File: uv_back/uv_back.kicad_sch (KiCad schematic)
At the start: 1 part, among them U1 OPA1656ID

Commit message: roughed out the schematic
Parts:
- added C1, C2: 0.1uF, Resistor_SMD:R_0603_1608Metric, symbol Device:C
- added C3, C5: 10000pF, Capacitor_SMD:C_0603_1608Metric, symbol Device:C
- added C4: 1uF, Capacitor_SMD:C_0805_2012Metric, symbol Device:C
- added J1, J3, J7: B2B-PH-SM4-TB(LF)(SN), Connector_JST:JST_PH_B2B-PH-SM4-TB_1x02-1MP_P2.00mm_Vertical, symbol Connector_Generic:Conn_01x02
- added J2, J4, J5, J6, J8: B3B-PH-SM4-TB(LF)(SN), Connector_JST:JST_PH_B3B-PH-SM4-TB_1x03-1MP_P2.00mm_Vertical, symbol Connector_Generic:Conn_01x03
- added R1, R2: 10k, Resistor_SMD:R_0603_1608Metric, symbol Device:R_US
- added R10, R6, R8, R9: 2k, Resistor_SMD:R_0603_1608Metric, symbol Device:R_US
- added R11: 50, Resistor_SMD:R_0603_1608Metric, symbol Device:R_US
- added R3, R4: 0, Resistor_SMD:R_0603_1608Metric, symbol Device:R_US
- added R5, R7: 1k, Resistor_SMD:R_0603_1608Metric, symbol Device:R_US
- added U2: OPA1656ID, Package_SO:SOIC-8_3.9x4.9mm_P1.27mm, symbol eAudio_OpAmp:OPA1656ID
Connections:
- net at U1.1: now also C3.2, C4.1, R9.2
- net at U1.2 (-): now also C3.1, J5.2 (Pin_2), J6.2 (Pin_2), R9.1
- net VMID: now reaches U1.3 (+)
- net VMID: now also J2.3 (Pin_3), J4.3 (Pin_3), U2.1, U2.2 (-)
- net GND: now reaches U1.4 (V-)
- net GND: now also C1.1, C2.1, C5.1, J1.2 (Pin_2), J3.2 (Pin_2), J8.3 (Pin_3), R10.1, R2.1, U2.4 (V-)
- net +9V: now reaches U1.8 (V+)
- net +9V: now also C1.2, C2.2, J7.1 (Pin_1), R1.2, U2.8 (V+)
- net at U1.5 (+): now also J2.2 (Pin_2)
- net at U1.6 (-): now also U1.7, R3.1
- new net: C4.2, R10.2, R11.1
- new net: R3.2, R5.1, R6.1
- new net: J5.1 (Pin_1), R5.2
- new net: J1.1 (Pin_1), J2.1 (Pin_1)
- new net: R4.1, U2.6 (-), U2.7
- new net: R4.2, R7.1, R8.1
- new net: J3.1 (Pin_1), J4.1 (Pin_1)
- new net: J4.2 (Pin_2), U2.5 (+)
- new net: C5.2, R1.1, R2.2, U2.3 (+)
- new net: J6.1 (Pin_1), R7.2
- new net: J6.3 (Pin_3), R8.2
- new net: J5.3 (Pin_3), R6.2
- new net BATT-: J7.2 (Pin_2), J8.2 (Pin_2)
- new net SIG_OUT: J8.1 (Pin_1), R11.2
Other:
- note added: "MixMonkey"
- note added: "Ring"
- note added: "Sleeve"
- note added: "Tip"
- company: (none) -> Wavenumber LLC
- title: (none) -> MixMonkey
- moved on the sheet: U1A, U1B, U1C

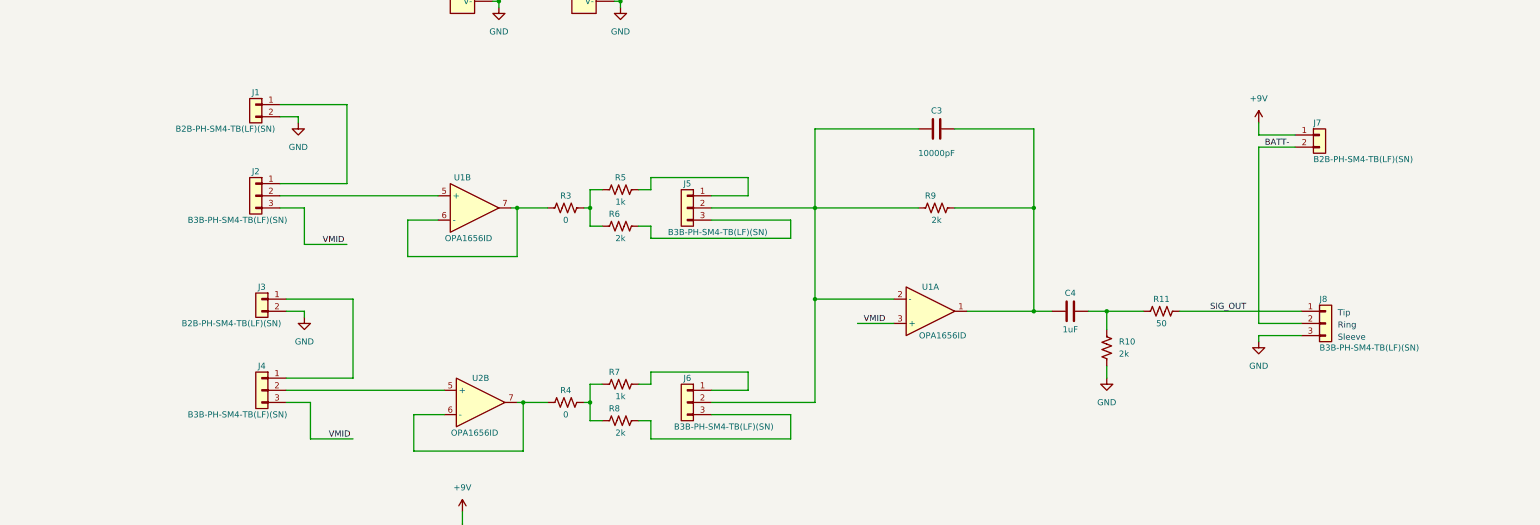
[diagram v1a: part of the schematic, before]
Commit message: connector and 3d model updates
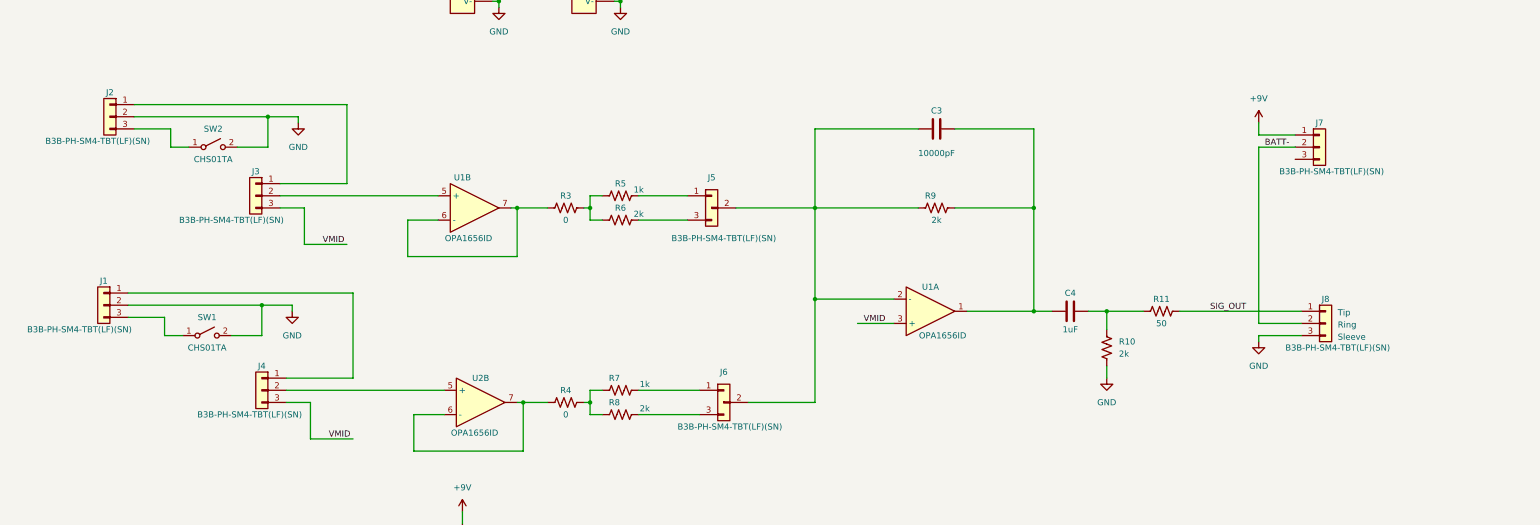
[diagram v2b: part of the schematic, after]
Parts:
- removed J1, J3, J7: B2B-PH-SM4-TB(LF)(SN), Connector_JST:JST_PH_B2B-PH-SM4-TB_1x02-1MP_P2.00mm_Vertical, symbol Connector_Generic:Conn_01x02
- removed J2, J4, J5, J6, J8: B3B-PH-SM4-TB(LF)(SN), Connector_JST:JST_PH_B3B-PH-SM4-TB_1x03-1MP_P2.00mm_Vertical, symbol Connector_Generic:Conn_01x03
- added J1, J2, J3, J4, J7, J8: B3B-PH-SM4-TBT(LF)(SN), eConnector_JST_PSH:B3B-PH-SM4, symbol eConnector_JST_PH:B3B-PH-SM4-TBT(LF)(SN)
- added J5, J6: B3B-PH-SM4-TBT(LF)(SN)_ALT, eConnector_JST_PSH:B3B-PH-SM4, symbol eConnector_JST_PH:B3B-PH-SM4-TBT(LF)(SN)_ALT
- added SW1, SW2: CHS01TA, eElectroMechanical:CHS-01TA, symbol eElectroMecahnical_Switch:CHS01TA
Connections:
- net +9V: now also J7.1 (Pin_1)
- net BATT-: now also J7.2 (Pin_2), J8.2 (Pin_2)
- net GND: now also J1.2 (Pin_2), J2.2 (Pin_2), J8.3 (Pin_3), SW1.2 (B), SW2.2 (B)
- net SIG_OUT: now also J8.1 (Pin_1)
- net VMID: now also J3.3 (Pin_3), J4.3 (Pin_3)
- net at C3.1, R9.1, U1.2 (-): now also J5.2 (Pin_2), J6.2 (Pin_2)
- net at R5.2: now also J5.1 (Pin_1)
- net at U1.5 (+): now also J3.2 (Pin_2)
- net at U2.5 (+): now also J4.2 (Pin_2)
- net at R7.2: now also J6.1 (Pin_1)
- net at R8.2: now also J6.3 (Pin_3)
- net at R6.2: now also J5.3 (Pin_3)
- new net: J1.1 (Pin_1), J4.1 (Pin_1)
- new net: J2.1 (Pin_1), J3.1 (Pin_1)
- new net: J2.3 (Pin_3), SW2.1 (A)
- new net: J1.3 (Pin_3), SW1.1 (A)
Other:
- moved on the sheet: R5, R6, R7, R8

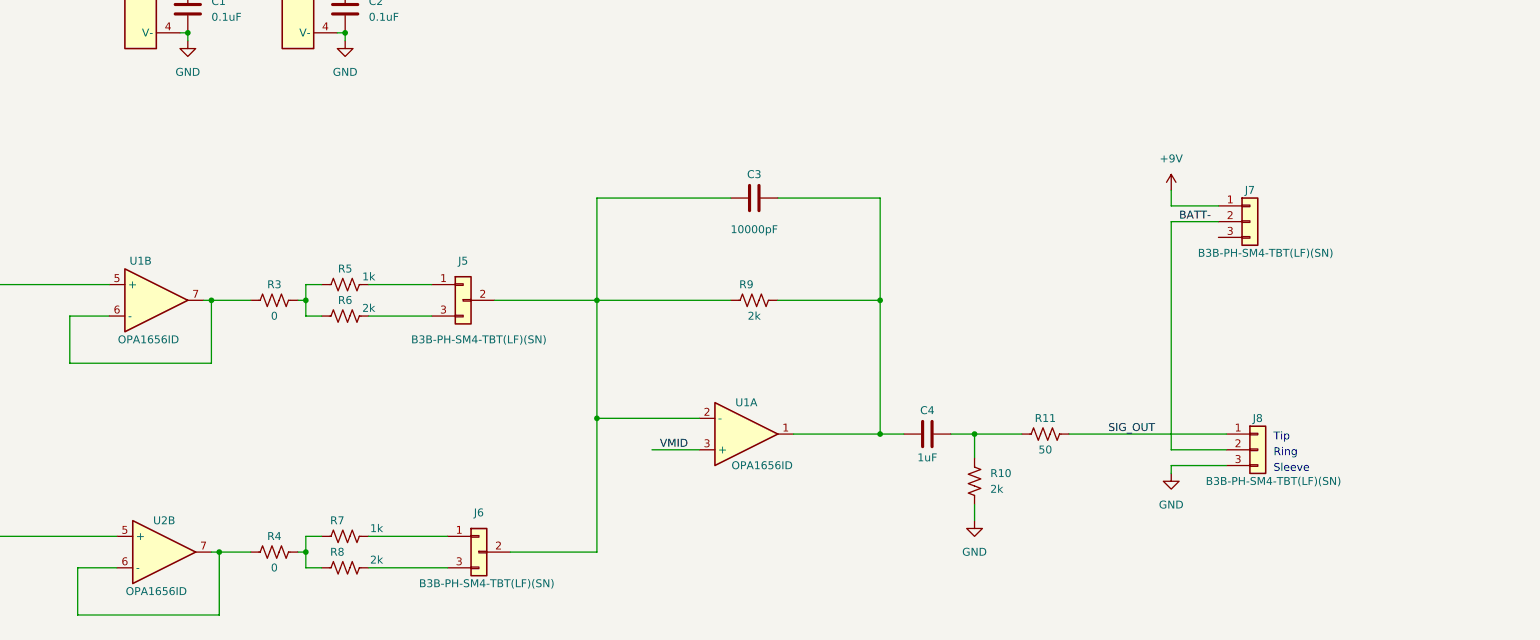
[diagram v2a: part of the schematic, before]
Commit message: 1st cut placement
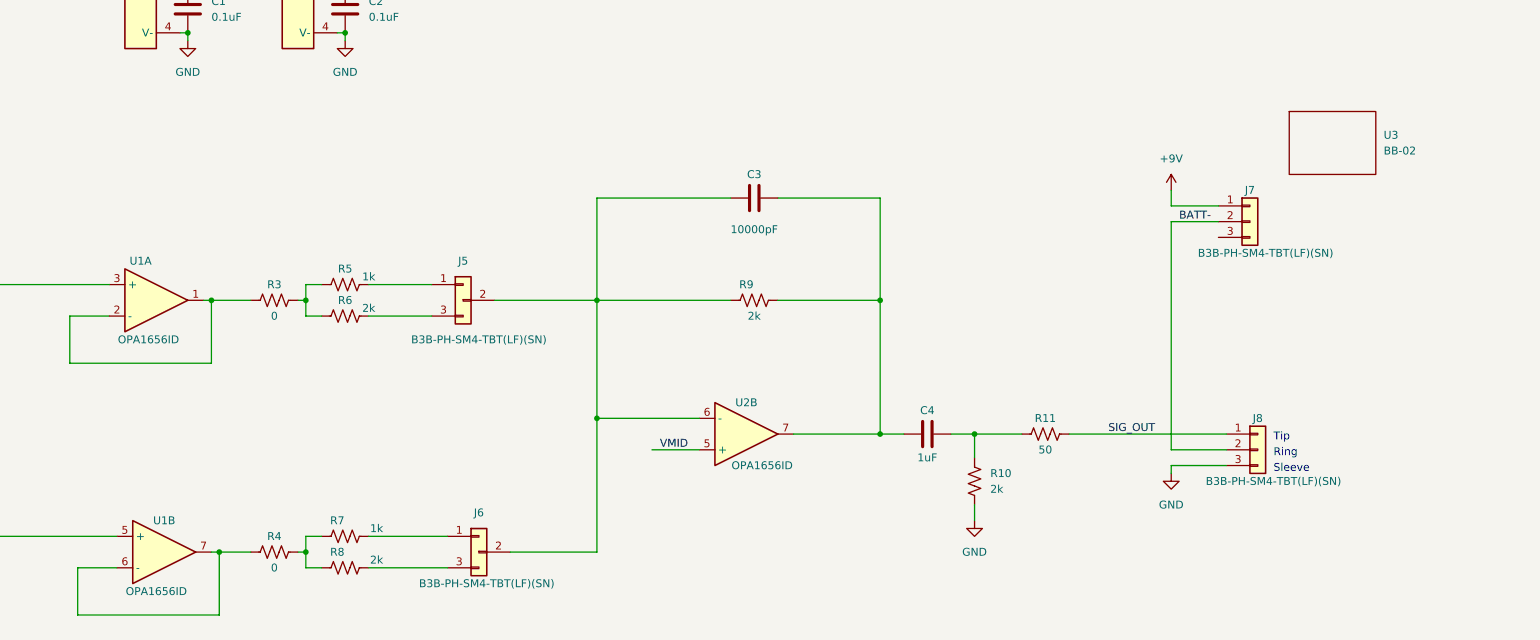
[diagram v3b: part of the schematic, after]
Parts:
- added U3: BB-02, eBattery:BB-04, symbol eBattery:BB-02
- C1, C2, R1, R10, R11, R2, R3, R4, R5, R6, R7, R8, R9: footprint Resistor_SMD:R_0603_1608Metric -> Resistor_SMD:R_0805_2012Metric_Pad1.20x1.40mm_HandSolder
- C3, C5: footprint Capacitor_SMD:C_0603_1608Metric -> Resistor_SMD:R_0805_2012Metric_Pad1.20x1.40mm_HandSolder
- C4: footprint Capacitor_SMD:C_0805_2012Metric -> Capacitor_SMD:C_0805_2012Metric_Pad1.18x1.45mm_HandSolder
- renumbered U2 to U1, U1 to U2
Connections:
- net VMID: now also U2.5 (+); no longer U2.3 (+)
- net at C3.2, C4.1, R9.2: now also U2.7; no longer U2.1
- net at C3.1, J5.2 (Pin_2), J6.2 (Pin_2)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: now also U2.6 (-); no longer U2.2 (-)
- net at J3.2 (Pin_2): now also U1.3 (+); no longer U1.5 (+)
- new net: R3.1, U1.1, U1.2 (-)

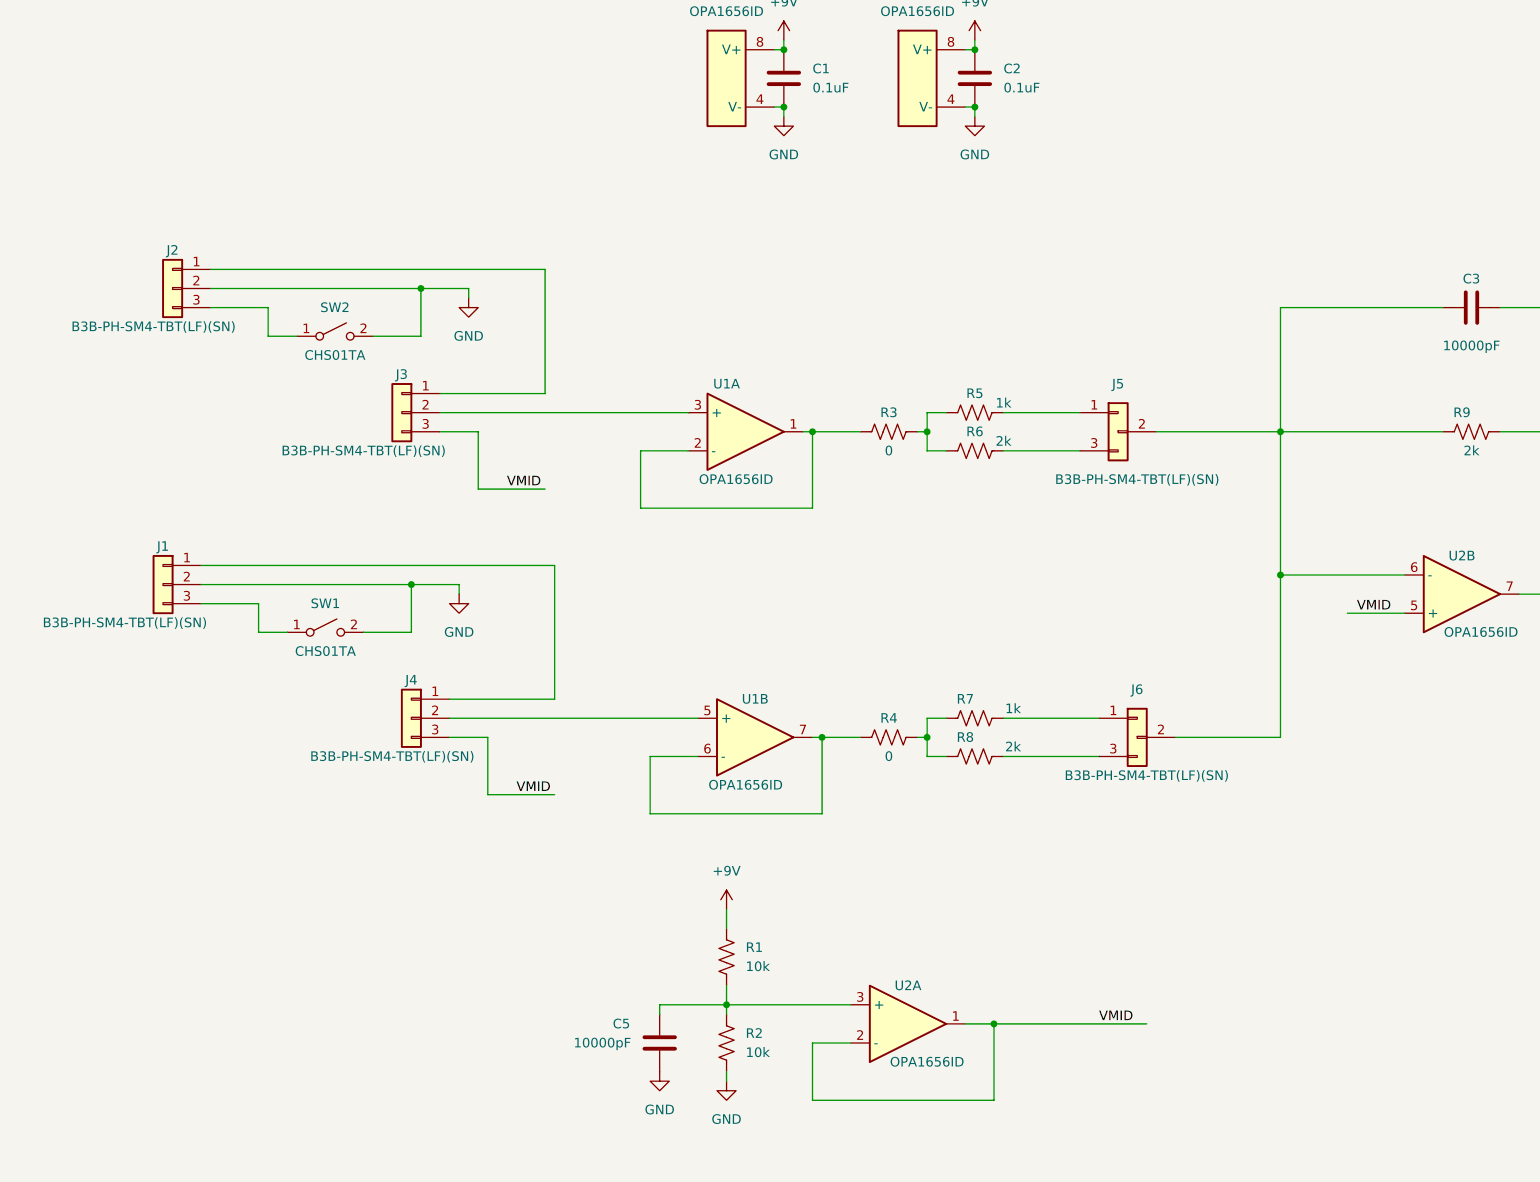
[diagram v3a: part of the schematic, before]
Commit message: Board Routed.   Need to Add Some Bling
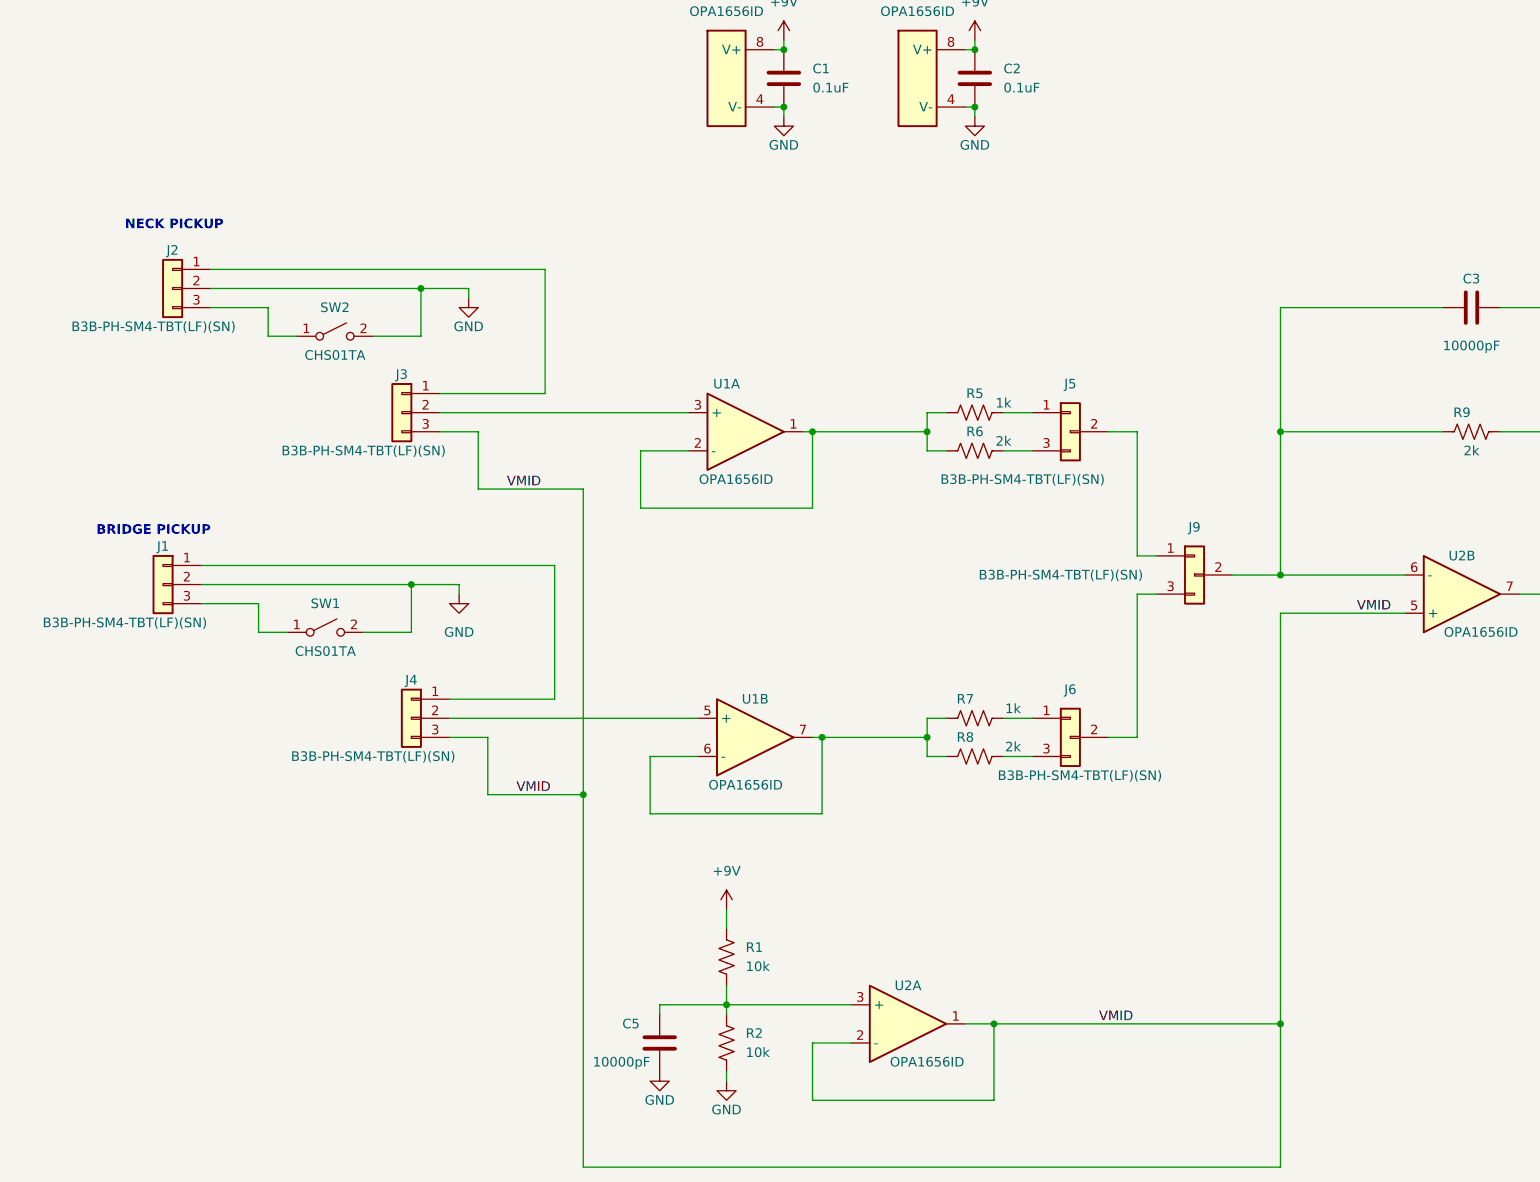
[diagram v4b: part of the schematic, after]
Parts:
- removed R3, R4: 0, Resistor_SMD:R_0805_2012Metric_Pad1.20x1.40mm_HandSolder, symbol Device:R_US
- added J9: B3B-PH-SM4-TBT(LF)(SN)_ALT, eConnector_JST:B3B-PH-SM4, symbol eConnector_JST_PH:B3B-PH-SM4-TBT(LF)(SN)_ALT
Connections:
- net at C3.1, R9.1, U2.6 (-): now also J9.2 (Pin_2); no longer J5.2 (Pin_2), J6.2 (Pin_2)
- net at R5.1, R6.1: now also U1.1, U1.2 (-)
- net at U1.6 (-), U1.7: now also R7.1, R8.1
- new net: J6.2 (Pin_2), J9.3 (Pin_3)
- new net: J5.2 (Pin_2), J9.1 (Pin_1)
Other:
- note added: "BRIDGE PICKUP"
- note added: "NECK PICKUP"
- moved on the sheet: J5, J6
